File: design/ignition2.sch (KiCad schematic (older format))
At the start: 9 parts, among them P14 CONN_1, P15 CONN_1, Q5 MOSFET_N, SW5 SWITCH_INV

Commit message: new ignition circuit, new usb-serial IC WARNING: The FT232RL doesnt support 125deg C
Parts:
- removed R32: 1k, R4-SM0805, symbol R
- removed SW5: SWITCH_INV, SIL-3, symbol SWITCH_INV
- added D?: DIODE, symbol DIODE
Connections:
- net labels removed: 5V_reg
- wire segments 15 -> 13
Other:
- moved on the sheet: P14, P15
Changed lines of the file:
@@
-EESchema Schematic File Version 2  date Fri 06 Aug 2010 10:16:31 PM ART
+EESchema Schematic File Version 2  date Sun 15 Aug 2010 12:57:33 PM ART
 LIBS:power
 LIBS:freeEMS_lib
@@
 EELAYER END
 $Descr A4 11700 8267
-Sheet 1 48
+Sheet 28 48
 Title "freeEMS 1.0"
-Date "7 aug 2010"
+Date "15 aug 2010"
 Rev "A.07"
 Comp "diyefi.org"
@@
 Comment4 ""
 $EndDescr
-Connection ~ 3400 2650
 Wire Wire Line
-	3400 2550 3400 2650
+	4300 2250 4100 2250
+Connection ~ 4100 1750
 Wire Wire Line
-	1750 1350 1950 1350
+	4200 1750 4100 1750
 Wire Wire Line
-	3050 1650 3050 1450
-Connection ~ 4100 1450
+	4100 1650 4100 1850
 Wire Wire Line
-	3550 1450 5100 1450
+	4100 1650 4050 1650
+Connection ~ 3400 2050
 Wire Wire Line
-	5100 1450 5100 2200
+	3550 1650 3650 1650
 Wire Wire Line
-	5100 2200 5300 2200
+	2750 2650 4100 2650
 Wire Wire Line
-	4100 1450 4100 1850
+	3350 2050 3800 2050
 Wire Wire Line
-	3050 1450 2950 1450
+	2800 2050 2850 2050
 Wire Wire Line
 	4100 2650 4100 2250
 Wire Wire Line
-	2800 2050 2850 2050
+	3050 1450 3050 1650
 Wire Wire Line
-	3800 2050 3350 2050
+	3400 2550 3400 2650
+Connection ~ 3400 2650
 Wire Wire Line
-	2750 2650 5300 2650
-Connection ~ 4100 2650
+	4200 1450 2950 1450
+Connection ~ 3050 1450
 Wire Wire Line
-	4050 1650 4100 1650
-Connection ~ 4100 1650
-Wire Wire Line
-	3550 1650 3650 1650
-Wire Wire Line
-	1750 1550 1950 1550
-Connection ~ 3400 2050
+	4100 1850 4300 1850
+$Comp
+L DIODE D?
+U 1 1 4C66EF37
+P 4300 2050
+F 0 "D?" H 4300 2150 40  0000 C CNN
+F 1 "DIODE" H 4300 1950 40  0000 C CNN
+	1    4300 2050
+	0    -1   -1   0
+$EndComp
 $Comp
 L PIP-3104 Q5
@@
 	1    3400 2300
 	-1   0    0    1
-$EndComp
-$Comp
-L SWITCH_INV SW5
-U 1 1 4C2F5328
-P 2450 1450
-F 0 "SW5" H 2250 1600 50  0000 C CNN
-F 1 "SWITCH_INV" H 2300 1300 50  0000 C CNN
-F 2 "SIL-3" H 2350 1700 60  0001 C CNN
-	1    2450 1450
-	-1   0    0    -1
 $EndComp
 $Comp
@@
 L CONN_1 P15
 U 1 1 48AA1A4E
-P 5450 2650
-F 0 "P15" H 5530 2650 40  0000 L CNN
-F 1 "CONN_1" H 5450 2705 30  0001 C CNN
-F 2 "1PIN" V 1880 2850 60  0001 C CNN
-	1    5450 2650
+P 4350 1750
+F 0 "P15" H 4430 1750 40  0000 L CNN
+F 1 "CONN_1" H 4350 1805 30  0001 C CNN
+F 2 "1PIN" V 780 1950 60  0001 C CNN
+	1    4350 1750
 	1    0    0    -1
 $EndComp
@@
 L CONN_1 P14
 U 1 1 4C2F5312
-P 5450 2200
-F 0 "P14" H 5530 2200 40  0000 L CNN
-F 1 "CONN_1" H 5450 2255 30  0001 C CNN
-F 2 "1PIN" V 1880 2600 60  0001 C CNN
-	1    5450 2200
+P 4350 1450
+F 0 "P14" H 4430 1450 40  0000 L CNN
+F 1 "CONN_1" H 4350 1505 30  0001 C CNN
+F 2 "1PIN" V 780 1850 60  0001 C CNN
+	1    4350 1450
 	1    0    0    -1
 $EndComp
-Text HLabel 1750 1550 0    60   Input ~ 0
-5V_reg
 $Comp
 L R R31
@@
 	0    1    1    0
 $EndComp
-$Comp
-L R R32
-U 1 1 4C2F52E1
-P 3300 1450
-F 0 "R32" V 3380 1450 50  0000 C CNN
-F 1 "1k" V 3300 1450 50  0000 C CNN
-F 2 "R4-SM0805" V 3480 1550 60  0001 C CNN
-F 4 "newark,38k0327" V 1130 2350 60  0001 C CNN "Field1"
-F 5 "vendor1, smd w hem" V 1130 2350 60  0001 C CNN "Field2"
-F 6 "vendor2, thru w hem" V 1130 2350 60  0001 C CNN "Field3"
-F 7 "vendor2, smd w hem" V 1130 2350 60  0001 C CNN "Field4"
-F 8 "250,mW" V 1130 2350 60  0001 C CNN "Field5"
-F 9 "5,%" V 1130 2350 60  0001 C CNN "Field6"
-F 10 "carbon film" V 1130 2350 60  0001 C CNN "Field7"
-F 11 "other,more,stuff" V 1130 2350 60  0001 C CNN "Field8"
-	1    3300 1450
-	0    1    1    0
-$EndComp
-Text HLabel 1750 1350 0    60   Input ~ 0
+Text HLabel 2950 1450 0    60   Input ~ 0
 12V_bat
 Text HLabel 2750 2650 0    60   BiDi ~ 0

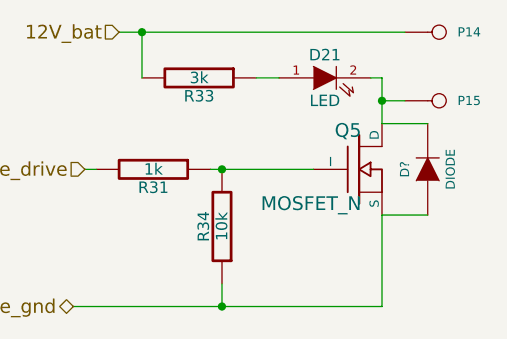
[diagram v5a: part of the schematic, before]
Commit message: now with 8 low Z injector drivers, BDM connector, FT232RL. 3 grounds: digital and analog, and power (isolated). I have to remove 2 ign drivers and rearrange the connector board pins.
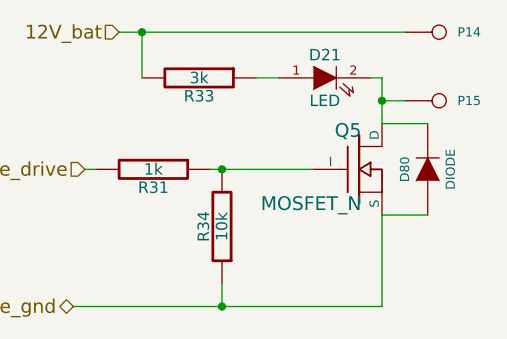
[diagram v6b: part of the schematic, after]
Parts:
- gave numbers to parts that had none: 1
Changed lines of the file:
@@
-EESchema Schematic File Version 2  date Sun 15 Aug 2010 12:57:33 PM ART
+EESchema Schematic File Version 2  date Sun 29 Aug 2010 06:27:37 AM ART
 LIBS:power
 LIBS:freeEMS_lib
@@
 EELAYER END
 $Descr A4 11700 8267
-Sheet 28 48
+Sheet 28 50
 Title "freeEMS 1.0"
-Date "15 aug 2010"
+Date "29 aug 2010"
 Rev "A.07"
 Comp "diyefi.org"
@@
 	4100 1850 4300 1850
 $Comp
-L DIODE D?
+L DIODE D80
 U 1 1 4C66EF37
 P 4300 2050
-F 0 "D?" H 4300 2150 40  0000 C CNN
+F 0 "D80" H 4300 2150 40  0000 C CNN
 F 1 "DIODE" H 4300 1950 40  0000 C CNN
 	1    4300 2050
